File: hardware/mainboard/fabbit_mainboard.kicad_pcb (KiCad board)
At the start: 2 copper layers, 82 x 146 mm, 33 parts, among them J1 Samtec_ERF8-030-XX.X-DV_2x30_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, J2 MECH_microSD_12x11.5, J3 MECH_USB_C_MidMount_9x7.5, J4 MECH_HDMI_A_MidMount_15x11.9, J5 MECH_Header_2x10_RA, J6 MECH_Header_2x2_RA, J7 MECH_Header_2x10_RA, SW1 MECH_SW_4x4, SW10 MECH_SW_4x4, SW11 MECH_SW_4x4, SW2 MECH_SW_4x4, SW3 MECH_SW_4x4, SW4 MECH_SW_4x4, SW5 MECH_SW_4x4, SW6 MECH_SW_4x4, SW7 MECH_SW_4x4, SW8 MECH_SW_4x4, SW9 MECH_SW_4x4, U2 MECH_ESP32C3_MINI

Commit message: hw(mainboard): стойки M2.5, стек 9 мм, выключатель PCM12 (#4)
* hw(case): стойки M2.5, стек 9 мм и выключатель PCM12 в модели

* hw(mainboard): мезонин, стойки и выключатель PCM12 по модели корпуса

* hw(adc-mezzanine): отверстия под M2.5, стек 9 мм
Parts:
- added SW12: SW_SPDT_PCM12, Button_Switch_SMD:SW_SPDT_PCM12, F.Cu at (61.4, 100.3)
- moved MZ1 0.75 mm to (100.0, 106.5)

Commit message: hw(mainboard): стойки мезонина Würth, правила DRC (#5)
* hw(mainboard): стойки мезонина Würth вместо заглушки

* hw(mainboard): правила DRC для стоек мезонина
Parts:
- H7, H8: value MECH_Standoff_SMD_M2.5_H9 -> Mounting_Wuerth_WA-SMSI-M2.5_H9mm_9774090151; footprint fabbit_mech:MECH_Standoff_SMD_M2.5_H9 -> Mounting_Wuerth:Mounting_Wuerth_WA-SMSI-M2.5_H9mm_9774090151

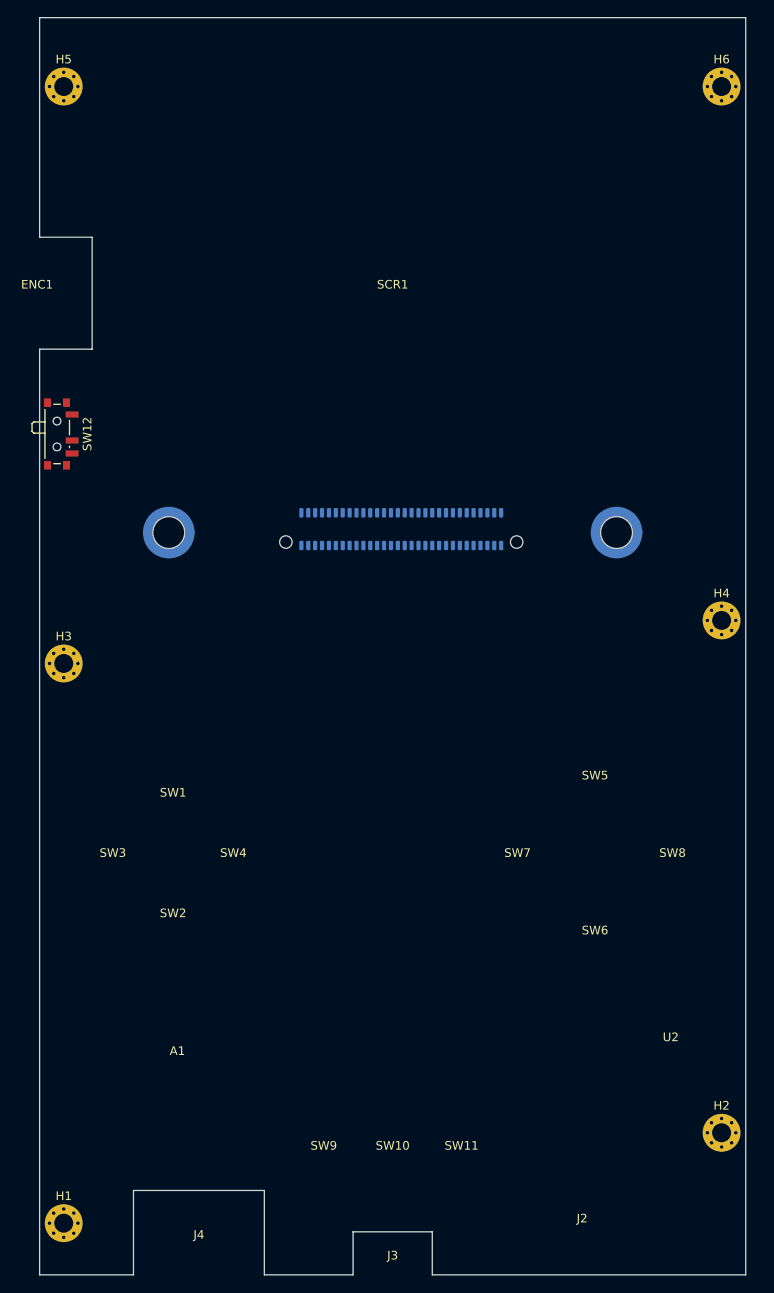
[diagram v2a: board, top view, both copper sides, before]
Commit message: hw(mainboard): контур 84,4×145,6×1,5, H1…H12, заглушки MECH по CSV
- H9…H12 под экраном: исключение courtyard в kicad_dru, на F под экраном пусто
- 11 заглушек прежнего корпуса убраны из fabbit_mech.pretty
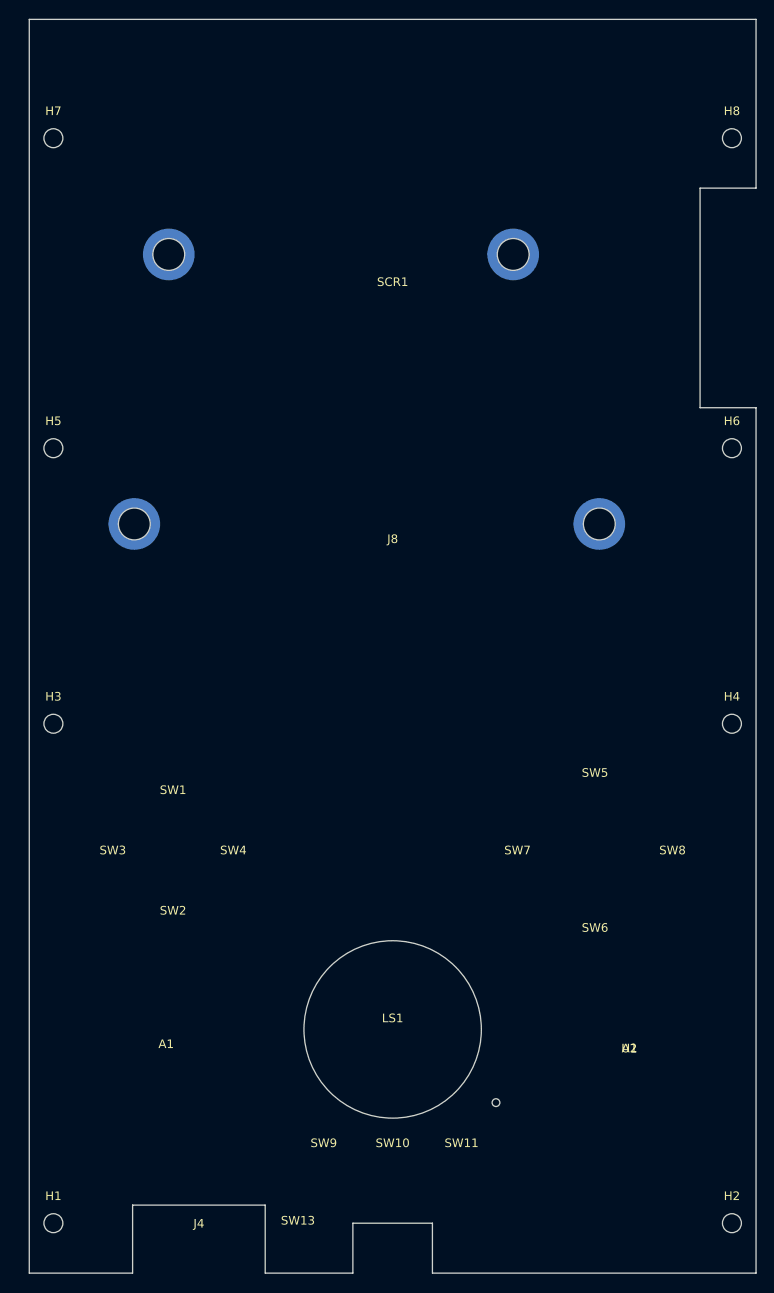
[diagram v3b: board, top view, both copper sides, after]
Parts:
- removed MZ1: MECH_Mezzanine_60x15, fabbit_mech:MECH_Mezzanine_60x15
- added A2: MECH_Area_F_MCU_25x16, fabbit_mech:MECH_Area_F_MCU_25x16, F.Cu at (127.5, 173.0)
- added A3: MECH_Area_B_Low_68x23.7, fabbit_mech:MECH_Area_B_Low_68x23.7, B.Cu at (100.0, 168.7)
- added A4: MECH_Area_B_Scoop_25x10.6, fabbit_mech:MECH_Area_B_Scoop_25x10.6, B.Cu at (97.5, 68.7)
- added A5: MECH_Area_B_LabPSU_28x13.5, fabbit_mech:MECH_Area_B_LabPSU_28x13.5, B.Cu at (100.0, 93.2)
- added A6: MECH_Area_B_Anlz_A_21.5x13.4, fabbit_mech:MECH_Area_B_Anlz_A_21.5x13.4, B.Cu at (74.2, 70.1)
- added A7: MECH_Area_B_Anlz_B_22x7.6, fabbit_mech:MECH_Area_B_Anlz_B_22x7.6, B.Cu at (123.0, 67.2)
- added A8: MECH_Battery_Tail_5x18, fabbit_mech:MECH_Battery_Tail_5x18, B.Cu at (137.5, 176.0)
- added H10: Mounting_Wuerth_WA-SMSI-M2.5_H9mm_9774090151, Mounting_Wuerth:Mounting_Wuerth_WA-SMSI-M2.5_H9mm_9774090151, B.Cu at (124.0, 110.8)
- added H11: Mounting_Wuerth_WA-SMSI-M2.5_H9mm_9774090151, Mounting_Wuerth:Mounting_Wuerth_WA-SMSI-M2.5_H9mm_9774090151, B.Cu at (74.0, 79.5)
- added H12: Mounting_Wuerth_WA-SMSI-M2.5_H9mm_9774090151, Mounting_Wuerth:Mounting_Wuerth_WA-SMSI-M2.5_H9mm_9774090151, B.Cu at (114.0, 79.5)
- added H9: Mounting_Wuerth_WA-SMSI-M2.5_H9mm_9774090151, Mounting_Wuerth:Mounting_Wuerth_WA-SMSI-M2.5_H9mm_9774090151, B.Cu at (70.0, 110.8)
- added HS1: MECH_Heat_Spreader_23x22, fabbit_mech:MECH_Heat_Spreader_23x22, B.Cu at (100.0, 131.0)
- added J8: MECH_FPC54_BXCONN, fabbit_mech:MECH_FPC54_BXCONN, F.Cu at (100.0, 113.8)
- added J9: MECH_MIPI20_FTSH_110_RA, fabbit_mech:MECH_MIPI20_FTSH_110_RA, B.Cu at (133.7, 54.8)
- added LS1: MECH_Speaker_D20, fabbit_mech:MECH_Speaker_D20, F.Cu at (100.0, 169.5)
- added M1: MECH_LRA_12x3.4, fabbit_mech:MECH_LRA_12x3.4, B.Cu at (59.7, 172.0)
- added MK1: MECH_Mic_SPH0641, fabbit_mech:MECH_Mic_SPH0641, B.Cu at (112.0, 178.0)
- added SW13: MECH_SW_3x4, fabbit_mech:MECH_SW_3x4, F.Cu at (89.0, 193.0)
- added U1: MECH_CH32H417_QFN128, fabbit_mech:MECH_CH32H417_QFN128, F.Cu at (127.5, 173.0)
- A1: value MECH_Area_PMIC_26x14 -> MECH_Area_F_Power_27.4x17; footprint fabbit_mech:MECH_Area_PMIC_26x14 -> fabbit_mech:MECH_Area_F_Power_27.4x17
- BT1: value MECH_Battery_65x40 -> MECH_Battery_70x40; footprint fabbit_mech:MECH_Battery_65x40 -> fabbit_mech:MECH_Battery_70x40
- ENC1: value MECH_Wheel_D12 -> MECH_Encoder_SIQ02; footprint fabbit_mech:MECH_Wheel_D12 -> fabbit_mech:MECH_Encoder_SIQ02; moved to B.Cu
- H1, H2, H3, H4, H5, H6: value MountingHole_2.2mm_M2_Pad_Via -> MountingHole_2.2mm_M2; footprint MountingHole:MountingHole_2.2mm_M2_Pad_Via -> MountingHole:MountingHole_2.2mm_M2
- H7, H8: value Mounting_Wuerth_WA-SMSI-M2.5_H9mm_9774090151 -> MountingHole_2.2mm_M2; footprint Mounting_Wuerth:Mounting_Wuerth_WA-SMSI-M2.5_H9mm_9774090151 -> MountingHole:MountingHole_2.2mm_M2; moved to F.Cu
- J1: value Samtec_ERF8-030-XX.X-DV_2x30_P0.8mm_Socket -> MECH_BergStak_2x40_9mm; footprint Connector_Samtec_EdgeRate:Samtec_ERF8-030-XX.X-DV_2x30_P0.8mm_Socket -> fabbit_mech:MECH_BergStak_2x40_9mm
- J2: value MECH_microSD_12x11.5 -> MECH_microSD_DM3AT; footprint fabbit_mech:MECH_microSD_12x11.5 -> fabbit_mech:MECH_microSD_DM3AT; moved to B.Cu
- J3: value MECH_USB_C_MidMount_9x7.5 -> MECH_USB_C_HCTL_24P; footprint fabbit_mech:MECH_USB_C_MidMount_9x7.5 -> fabbit_mech:MECH_USB_C_HCTL_24P; moved to B.Cu
- J4: value MECH_HDMI_A_MidMount_15x11.9 -> MECH_HDMI_A_HDGC_GD116; footprint fabbit_mech:MECH_HDMI_A_MidMount_15x11.9 -> fabbit_mech:MECH_HDMI_A_HDGC_GD116
- J5: value MECH_Header_2x10_RA -> MECH_Socket_DS1024_2x12_RA; footprint fabbit_mech:MECH_Header_2x10_RA -> fabbit_mech:MECH_Socket_DS1024_2x12_RA
- J6: value MECH_Header_2x2_RA -> MECH_Socket_DS1024_2x2_RA; footprint fabbit_mech:MECH_Header_2x2_RA -> fabbit_mech:MECH_Socket_DS1024_2x2_RA
- J7: value MECH_Header_2x10_RA -> MECH_Socket_DS1024_2x10_RA; footprint fabbit_mech:MECH_Header_2x10_RA -> fabbit_mech:MECH_Socket_DS1024_2x10_RA
- MOD1: value MECH_SODIMM_i9plus -> MECH_SODIMM_TE1473005_i9plus; footprint fabbit_mech:MECH_SODIMM_i9plus -> fabbit_mech:MECH_SODIMM_TE1473005_i9plus
- SW12: value SW_SPDT_PCM12 -> MECH_SW_SKRTLAE010; footprint Button_Switch_SMD:SW_SPDT_PCM12 -> fabbit_mech:MECH_SW_SKRTLAE010; moved to B.Cu
- U2: value MECH_ESP32C3_MINI -> MECH_ESP32C5_MINI1; footprint fabbit_mech:MECH_ESP32C3_MINI -> fabbit_mech:MECH_ESP32C5_MINI1; moved to B.Cu
- moved U2 91.9 mm to (131.6, 79.5)
- moved H7 47.7 mm to (60.6, 66.0)
- moved H8 47.7 mm to (139.4, 66.0)
- moved H5 42.0 mm to (60.6, 102.0)
- moved H6 42.0 mm to (139.4, 102.0)
- moved H4 12.1 mm to (139.4, 134.0)
- moved H2 10.6 mm to (139.4, 192.0)
- moved J7 10.5 mm to (108.5, 56.4), turned to 180 degrees
- moved MOD1 10.0 mm to (100.0, 140.0)
- moved SW12 9.26 mm to (59.9, 109.5), turned to 180 degrees
- moved J6 7.59 mm to (92.7, 56.4), turned to 180 degrees
- moved J5 7.14 mm to (74.5, 56.4), turned to 180 degrees
- moved H3 7.10 mm to (60.6, 134.0)
- moved J2 3.45 mm to (121.6, 189.0), turned to 180 degrees
- moved ENC1 3.00 mm to (61.7, 84.0), turned to 180 degrees
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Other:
- board size 82 x 146 mm -> 84.4 x 145.6 mm
